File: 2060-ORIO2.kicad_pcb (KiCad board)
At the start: 4 copper layers, 100 x 100 mm, 198 parts, among them J11 RaspberryPI-B+header, J12 Conn_01x04, J13 Conn_01x08, J14 Conn_01x02, J15 Conn_01x08, J16 Conn_01x10, J17 Conn_01x10, J18 Conn_01x10, J19 Conn_01x10, J20 Conn_01x09, J21 Conn_01x08, J22 Conn_01x08, J23 Conn_01x08, J24 Conn_01x08, J25 Conn_01x08, J26 Conn_01x08, J28 Conn_01x16, J29 Conn_01x16, J30 Conn_01x16, J31 Conn_01x08, J32 Conn_01x08, J33 Conn_01x08, J34 Conn_01x08, J35 TBL001-500-02GY-2GY, Q11 ULN2803ADWR, Q12 BCV27, Q91 BCV27, Q92 BCV27, Q93 BCV27, Q94 BCV27, SW1 SW_DIP_x01, SW11 SW_DIP_x08, U1 AOZ2151TQI-19, U11 ICE40HX4K-TQ144, U12 ‎74LVT245B, U13 ‎74LVT245B, U14 ‎74LVT245B, U15 AOZ2151TQI-19, U16 MCP3008, U17 AZ1117CH-3.3TRG1, U18 AZ1117CH-3.3TRG1, U19 AZ1117CH-1.2, U20 AOZ2151TQI-19, U21 ‎74LVT245B, U22 ‎74LVT245B, U23 ‎74LVT245B, U24 ‎74LVT245B, U26 AP3012, Y11 XLH536025_000000I

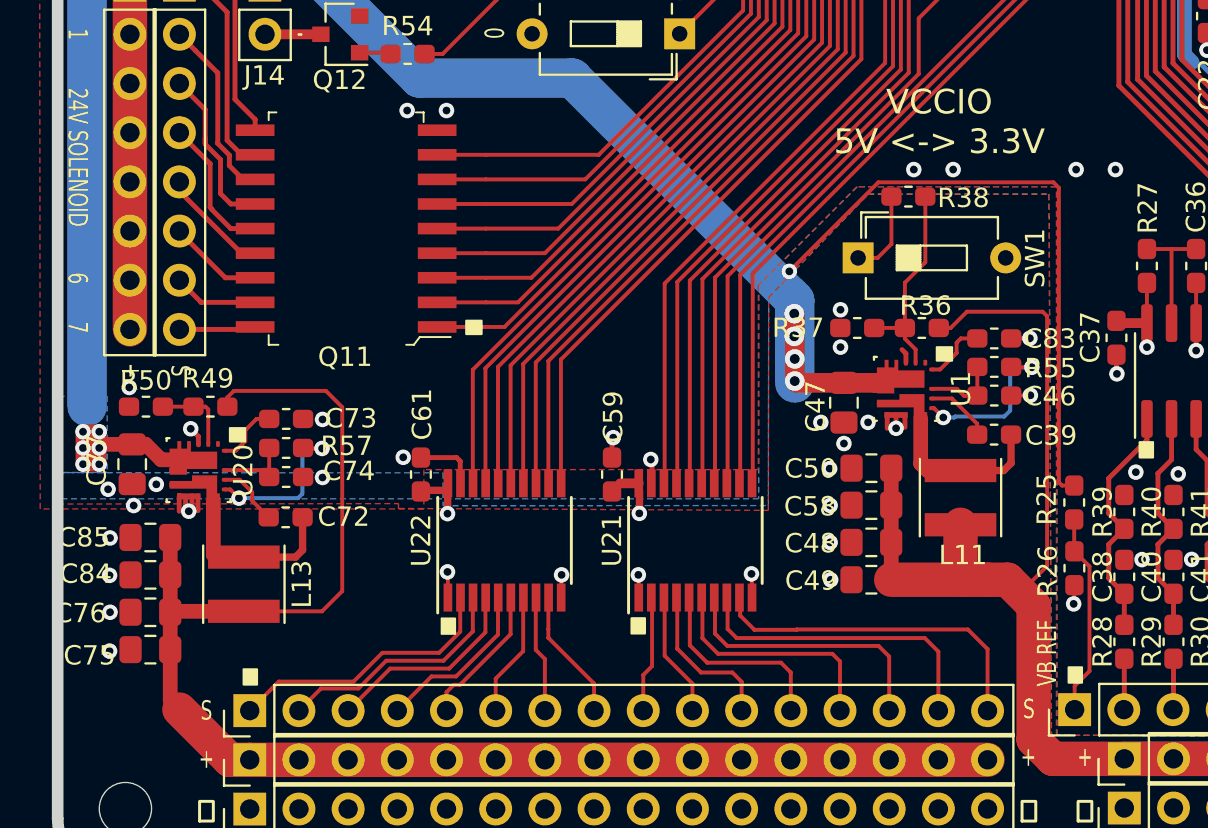
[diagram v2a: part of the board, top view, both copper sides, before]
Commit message: Change +BATT voltage divider to /6.
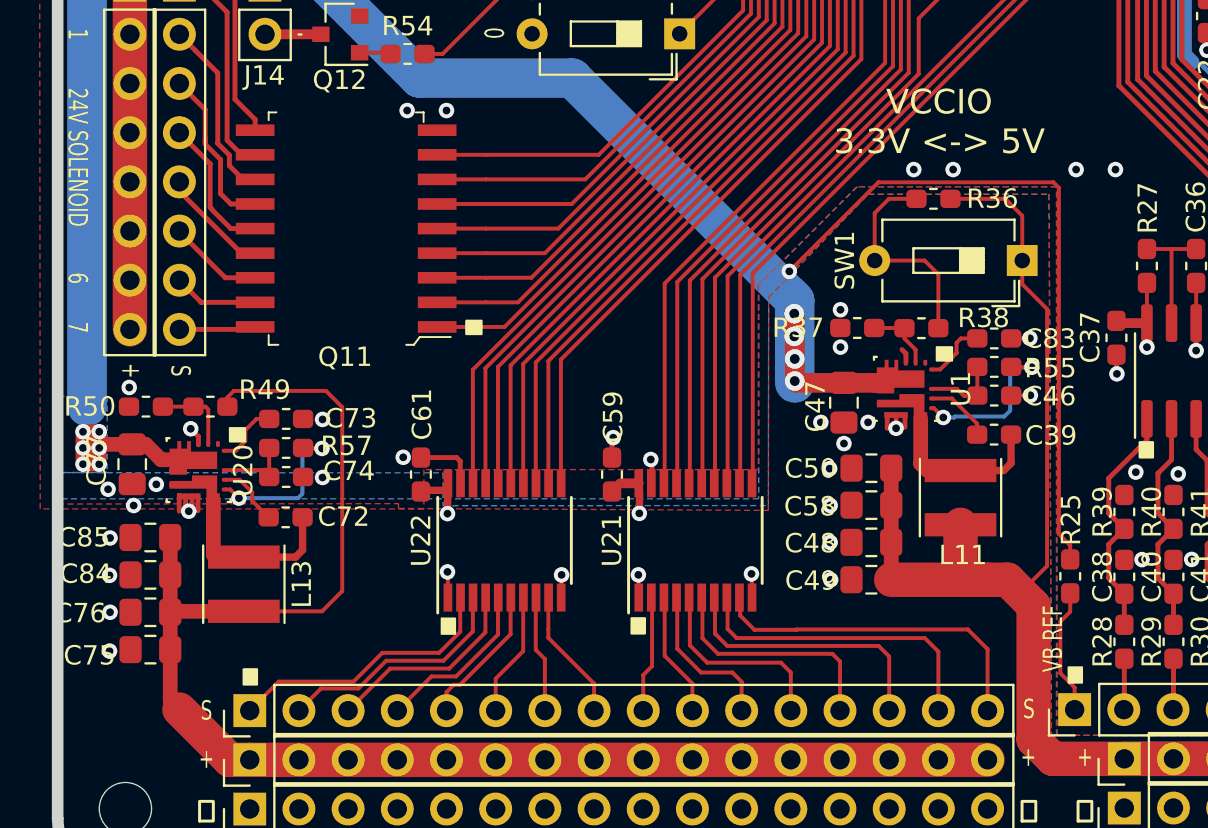
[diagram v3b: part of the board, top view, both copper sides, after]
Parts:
- removed R26: 3K3, Resistor_SMD:R_0603_1608Metric_Pad1.05x0.95mm_HandSolder
- R25: value 33K -> 18K8
- R36: value x -> 3K4
- R37, R48, R50: value x -> 1K6
- R38: value x -> 5K
- R47: value x -> 8K4
- R49: value x -> 10K4
- moved SW1 8.48 mm to (121.8, 110.2), turned to 180 degrees
- moved R38 6.83 mm to (116.6, 113.7)
- moved R36 6.69 mm to (117.2, 107.0), turned to 0 degrees
- moved R25 3.82 mm to (124.3, 126.5)
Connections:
- R36 pad 1: VCC_IO -> Net-(R36-Pad1)
- R36 pad 2: Net-(R36-Pad2) -> VCC_IO
- R37 pad 1: Net-(R36-Pad2) -> Net-(R37-Pad1)
- R38 pad 1: Net-(R38-Pad1) -> Net-(R37-Pad1)
- R38 pad 2: Net-(R36-Pad2) -> Net-(R36-Pad1)
- SW1 pad 1: Net-(R38-Pad1) -> VCC_IO
- SW1 pad 2: GND -> Net-(R36-Pad1)
- U1 pad 2: Net-(R36-Pad2) -> Net-(R37-Pad1)
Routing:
- net Net-(R36-Pad1): track 0.00 -> 11.3 mm
- net Net-(R36-Pad2): track 10.8 -> 0.00 mm
- net Net-(R38-Pad1): track 4.47 -> 0.00 mm
- net /VBATT_DIV: track 10.5 -> 6.52 mm
- net VCC_IO: track 314.0 -> 317.7 mm
- net Net-(R37-Pad1): track 0.00 -> 3.59 mm
- net +BATT: track 204.5 -> 207.9 mm
- net GND: track 112.0 -> 111.1 mm, vias 155 -> 154
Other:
- board text added: "VCCIO 3.3V <-> 5V"
- board text removed: "VCCIO 5V <-> 3.3V"

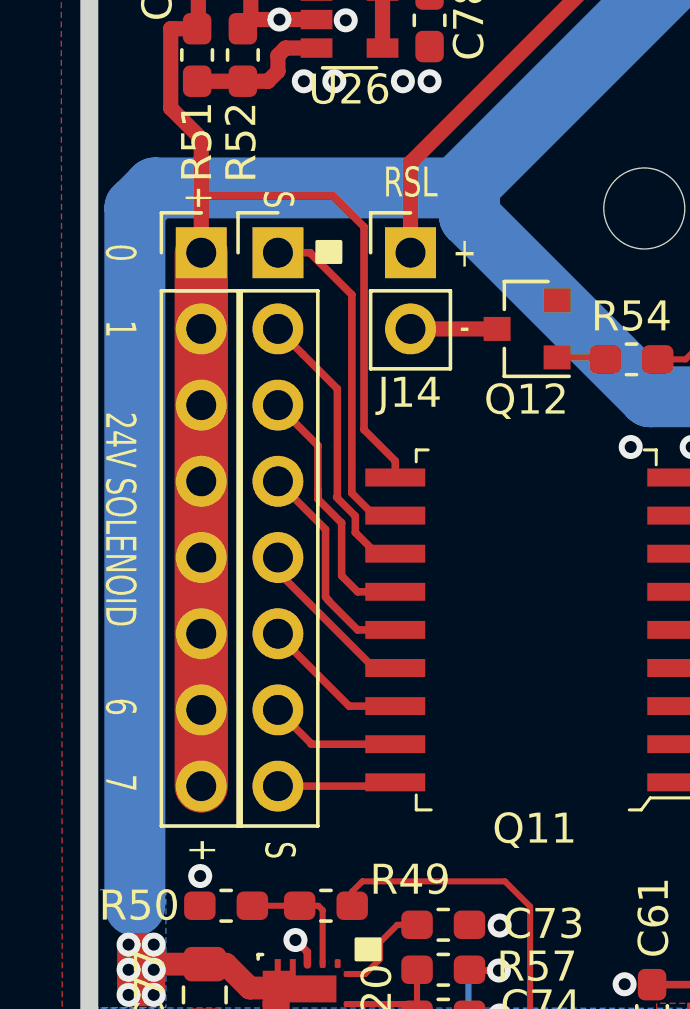
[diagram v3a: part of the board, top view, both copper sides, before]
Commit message: Adjust solenoid connector position.
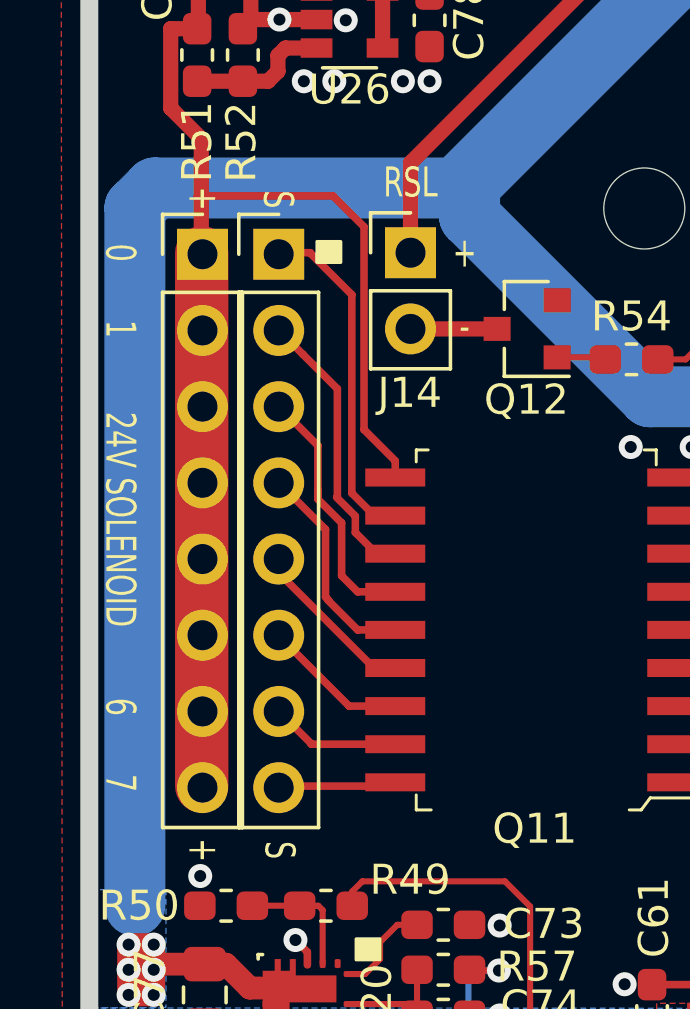
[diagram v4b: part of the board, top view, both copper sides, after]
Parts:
- R55, R56, R57: value x -> 0
- moved J13 0.07 mm to (75.8, 96.0)
- moved J15 0.06 mm to (78.3, 96.0)
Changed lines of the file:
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@@
-(kicad_pcb (version 20171130) (host pcbnew 5.1.6-c6e7f7d~87~ubuntu18.04.1)
+(kicad_pcb (version 20171130) (host pcbnew 5.1.5+dfsg1-2build2)
   (general
     (thickness 1.6)
     (drawings 165)
-    (tracks 2351)
+    (tracks 2352)
     (zones 0)
     (modules 197)
@@
       (effects (font (size 1 1) (thickness 0.15)))
     )
-    (fp_text value x (at 0 1.43) (layer F.Fab)
+    (fp_text value 0 (at 0 1.43) (layer F.Fab)
       (effects (font (size 1 1) (thickness 0.15)))
     )
@@
       (effects (font (size 1 1) (thickness 0.15)))
     )
-    (fp_text value x (at 0 1.43 90) (layer F.Fab)
+    (fp_text value 0 (at 0 1.43 90) (layer F.Fab)
       (effects (font (size 1 1) (thickness 0.15)))
     )
@@
       (effects (font (size 1 1) (thickness 0.15)))
     )
-    (fp_text value x (at 0 1.43) (layer F.Fab)
+    (fp_text value 0 (at 0 1.43) (layer F.Fab)
       (effects (font (size 1 1) (thickness 0.15)))
     )
@@
     )
   )
-  (module Connector_PinHeader_2.54mm:PinHeader_1x08_P2.54mm_Vertical (layer F.Cu)
-    (at 78.2878 95.975)
+  (module Connector_PinHeader_2.54mm:PinHeader_1x08_P2.54mm_Vertical locked (layer F.Cu)
+    (at 78.3132 96.0258)
     (descr "Through hole straight pin header, 1x08, 2.54mm pitch, single row")
     (tags "Through hole pin header THT 1x08 2.54mm single row")
@@
     )
   )
-  (module Connector_PinHeader_2.54mm:PinHeader_1x08_P2.54mm_Vertical (layer F.Cu)
-    (at 75.7326 95.975)
+  (module Connector_PinHeader_2.54mm:PinHeader_1x08_P2.54mm_Vertical locked (layer F.Cu)
+    (at 75.7732 96.0258)
     (descr "Through hole straight pin header, 1x08, 2.54mm pitch, single row")
     (tags "Through hole pin header THT 1x08 2.54mm single row")
@@
     (effects (font (size 1 0.7) (thickness 0.15)))
   )
-  (gr_text + (at 75.6716 94.1462 270) (layer F.SilkS)
+  (gr_text + (at 75.7986 94.1716 270) (layer F.SilkS)
     (effects (font (size 1 0.7) (thickness 0.15)))
   )
@@
   (segment (start 82.9323 44.8067) (end 84.5883 44.8067) (width 0.2032) (layer F.Cu) (net 278))
   (segment (start 83.6182 65.749) (end 86.238 65.749) (width 2.54) (layer F.Cu) (net 279))
-  (segment (start 75.7326 113.755) (end 75.7326 95.975) (width 1.778) (layer F.Cu) (net 280))
+  (segment (start 75.7478 113.755) (end 75.7478 95.975) (width 1.778) (layer F.Cu) (net 280))
   (segment (start 76.3574 85.221) (end 76.0878 85.221) (width 0.508) (layer F.Cu) (net 280))
   (segment (start 75.6348 85.674) (end 75.6348 86.958) (width 0.508) (layer F.Cu) (net 280))
@@
   (segment (start 75.5954 88.5087) (end 74.71399 88.5087) (width 0.508) (layer F.Cu) (net 280))
   (segment (start 75.7326 92.1752) (end 75.7326 94.0802) (width 0.508) (layer F.Cu) (net 280))
-  (segment (start 75.7326 94.0802) (end 75.7326 95.975) (width 0.508) (layer F.Cu) (net 280))
   (segment (start 82.1984 102.914) (end 82.1984 103.468) (width 0.254) (layer F.Cu) (net 280))
   (segment (start 81.158 101.8736) (end 82.1984 102.914) (width 0.254) (layer F.Cu) (net 280))
@@
   (segment (start 80.1268 94.0802) (end 81.158 95.1114) (width 0.254) (layer F.Cu) (net 280))
   (segment (start 75.7326 94.0802) (end 80.1268 94.0802) (width 0.254) (layer F.Cu) (net 280))
+  (segment (start 75.7326 95.4568) (end 75.2398 95.9496) (width 0.508) (layer F.Cu) (net 280))
+  (segment (start 75.7326 94.0802) (end 75.7326 95.4568) (width 0.508) (layer F.Cu) (net 280))
   (segment (start 82.7074 98.515) (end 85.5936 98.515) (width 0.508) (layer F.Cu) (net 281))
   (segment (start 89.1324 99.465) (end 89.1984 99.531) (width 0.2032) (layer F.Cu) (net 282))

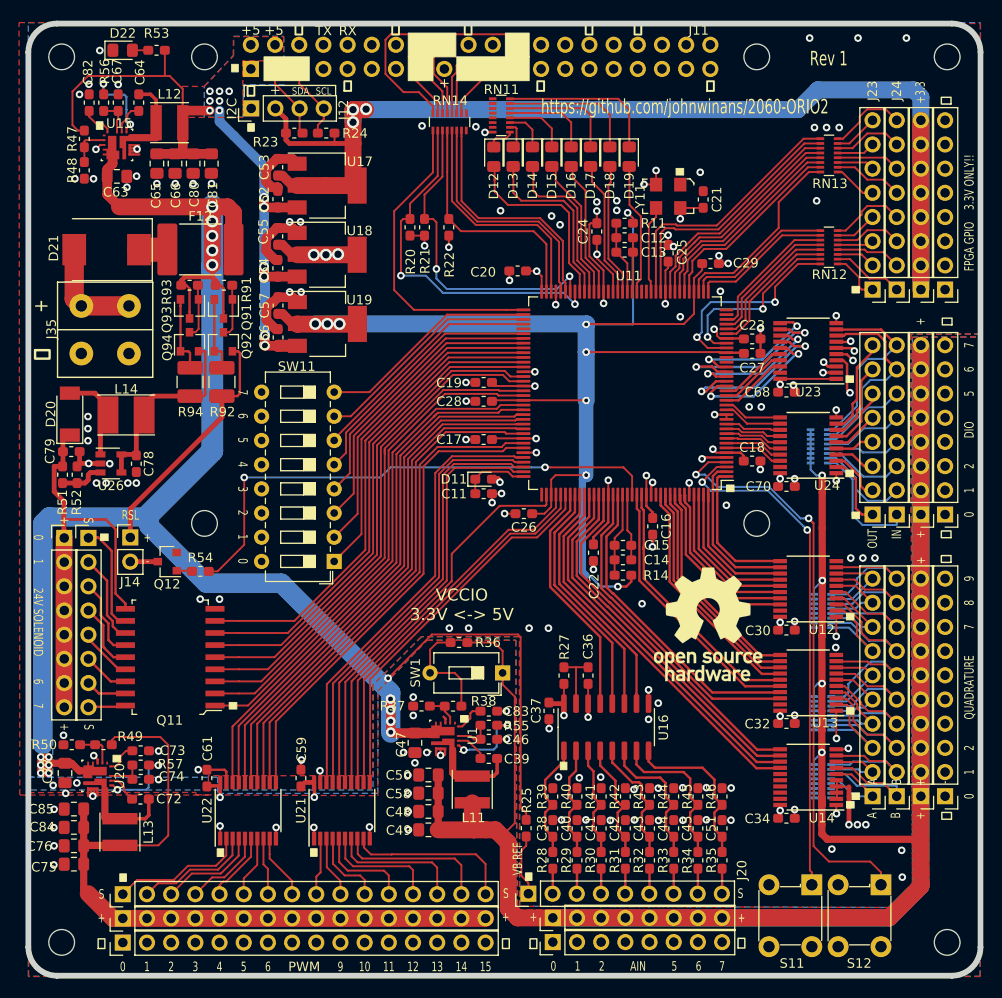
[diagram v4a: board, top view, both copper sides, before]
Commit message: Replace AOZ2151TQI-19 regulators with AP63300WU-7
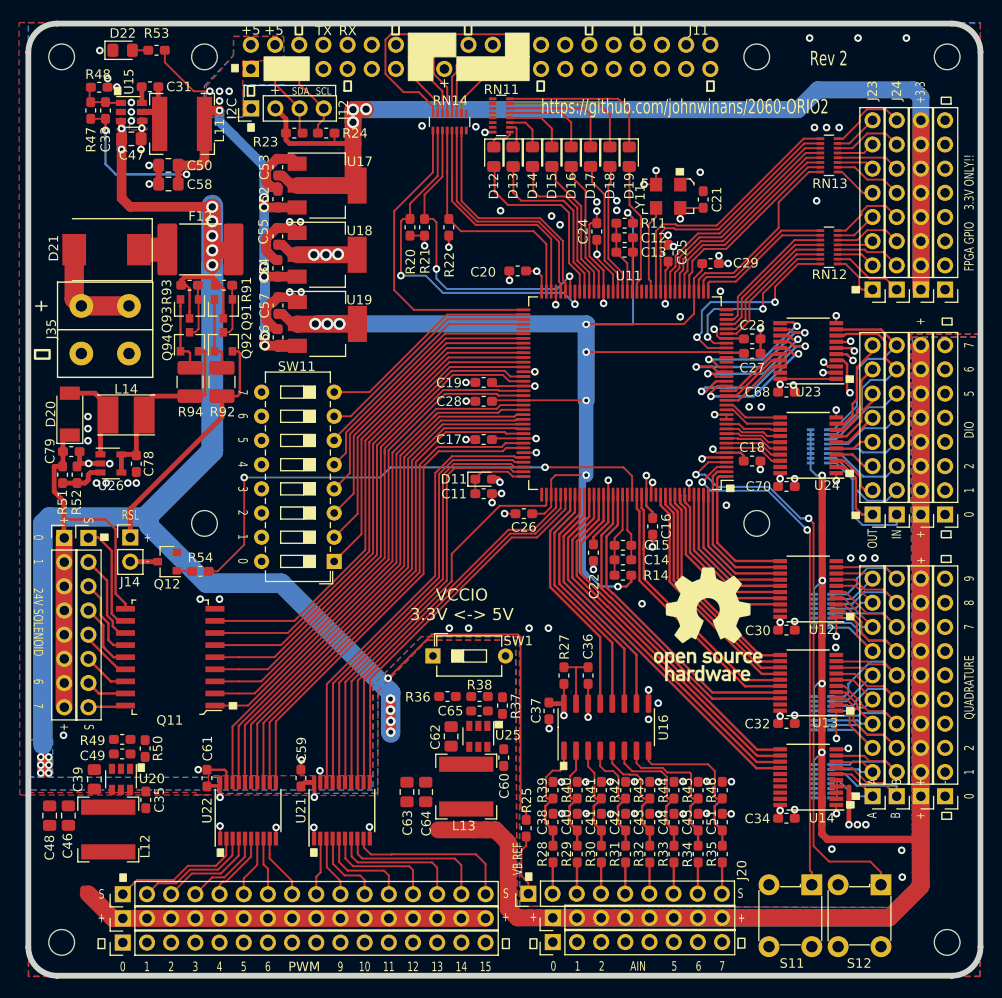
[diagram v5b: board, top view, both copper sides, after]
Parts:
- removed C66, C75, C76, C77, C80, C81, C84, C85: 22uF, Capacitor_SMD:C_0805_2012Metric_Pad1.15x1.40mm_HandSolder
- removed C67, C74: 4.7uF, Capacitor_SMD:C_0603_1608Metric_Pad1.05x0.95mm_HandSolder
- removed C72: .1uF, Capacitor_SMD:C_0603_1608Metric_Pad1.05x0.95mm_HandSolder
- removed C73, C82, C83: .001uF, Capacitor_SMD:C_0603_1608Metric_Pad1.05x0.95mm_HandSolder
- removed R55, R56, R57: 0, Resistor_SMD:R_0603_1608Metric_Pad1.05x0.95mm_HandSolder
- removed U1: AOZ2151TQI-19, jb-footprint:AOZ2151TQI-19
- added C31: .1uF, Capacitor_SMD:C_0603_1608Metric_Pad1.05x0.95mm_HandSolder, F.Cu at (84.8, 48.6)
- added C33: 47pF, Capacitor_SMD:C_0603_1608Metric_Pad1.05x0.95mm_HandSolder, F.Cu at (80.1, 51.1)
- added C35: .1uF, Capacitor_SMD:C_0603_1608Metric_Pad1.05x0.95mm_HandSolder, F.Cu at (84.3, 123.5)
- added C60: .1uF, Capacitor_SMD:C_0603_1608Metric_Pad1.05x0.95mm_HandSolder, F.Cu at (121.9, 119.1)
- added C62: 10uF, Capacitor_SMD:C_0805_2012Metric_Pad1.15x1.40mm_HandSolder, F.Cu at (116.4, 116.9)
- added U25: AP63300, Package_TO_SOT_SMD:SOT-23-6, F.Cu at (119.3, 116.9)
- C39: value .1uF -> 10uF; footprint Capacitor_SMD:C_0603_1608Metric_Pad1.05x0.95mm_HandSolder -> Capacitor_SMD:C_0805_2012Metric_Pad1.15x1.40mm_HandSolder
- C46: value 4.7uF -> 22uF; footprint Capacitor_SMD:C_0603_1608Metric_Pad1.05x0.95mm_HandSolder -> Capacitor_SMD:C_0805_2012Metric_Pad1.15x1.40mm_HandSolder
- C47: value 22uF -> 10uF
- C49, C65: value 22uF -> 47pF; footprint Capacitor_SMD:C_0805_2012Metric_Pad1.15x1.40mm_HandSolder -> Capacitor_SMD:C_0603_1608Metric_Pad1.05x0.95mm_HandSolder
- C64: value .1uF -> 22uF; footprint Capacitor_SMD:C_0603_1608Metric_Pad1.05x0.95mm_HandSolder -> Capacitor_SMD:C_0805_2012Metric_Pad1.15x1.40mm_HandSolder
- L11, L12, L13: value 2.2uH -> 6.8uH; footprint Inductor_SMD:L_Taiyo-Yuden_MD-4040 -> Inductor_SMD:L_Bourns-SRN6028
- U15, U20: value AOZ2151TQI-19 -> AP63300; footprint jb-footprint:AOZ2151TQI-19 -> Package_TO_SOT_SMD:SOT-23-6
- moved C64 78.4 mm to (113.7, 122.7)
- moved L11 76.3 mm to (88.1, 52.5), turned to 0 degrees
- moved L12 74.5 mm to (80.4, 126.6), turned to 270 degrees
- moved C63 71.5 mm to (111.8, 122.7), turned to 90 degrees
- moved C47 70.1 mm to (82.8, 54.1), turned to 0 degrees
- moved C50 69.6 mm to (86.7, 56.9)
- moved C58 69.6 mm to (86.7, 58.9)
- moved C65 66.7 mm to (119.4, 114.2), turned to 0 degrees
- moved C46 44.9 mm to (76.2, 125.2), turned to 90 degrees
- moved C39 41.5 mm to (78.9, 121.4), turned to 270 degrees
- moved C48 39.8 mm to (74.2, 125.2), turned to 90 degrees
- moved L13 36.7 mm to (118.0, 122.1)
- moved C49 33.1 mm to (81.9, 118.7), turned to 0 degrees
- moved R48 8.86 mm to (79.4, 48.7), turned to 0 degrees
- moved R37 8.51 mm to (121.8, 113.6), turned to 270 degrees
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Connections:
- C39 pad 1: Net-(C39-Pad1) -> +BATT
- C39 pad 2: Net-(C39-Pad2) -> GND
- C46 pad 1: Net-(C46-Pad1) -> VCC_PWM
- C48 pad 1: VCC_IO -> VCC_PWM
- C49 pad 1: VCC_IO -> VCC_PWM
- C49 pad 2: GND -> Net-(C49-Pad2)
- C50 pad 1: VCC_IO -> 5V_PI
- C58 pad 1: VCC_IO -> 5V_PI
- C63 pad 1: +BATT -> VCC_IO
- C64 pad 1: Net-(C64-Pad1) -> VCC_IO
- C64 pad 2: Net-(C64-Pad2) -> GND
- C65 pad 1: 5V_PI -> VCC_IO
- C65 pad 2: GND -> Net-(C65-Pad2)
- L11 pad 1: Net-(C39-Pad2) -> Net-(C31-Pad2)
- L11 pad 2: VCC_IO -> 5V_PI
- L12 pad 1: Net-(C64-Pad2) -> Net-(C35-Pad2)
- L12 pad 2: 5V_PI -> VCC_PWM
- L13 pad 1: Net-(C72-Pad2) -> Net-(C60-Pad2)
- L13 pad 2: VCC_PWM -> VCC_IO
- R37 pad 1: Net-(R37-Pad1) -> Net-(C65-Pad2)
- R38 pad 1: Net-(R37-Pad1) -> Net-(C65-Pad2)
- R47 pad 2: Net-(R47-Pad2) -> Net-(C33-Pad2)
- R48 pad 1: Net-(R47-Pad2) -> Net-(C33-Pad2)
- R49 pad 2: Net-(R49-Pad2) -> Net-(C49-Pad2)
- R50 pad 1: Net-(R49-Pad2) -> Net-(C49-Pad2)
- U15 pad 1: Net-(U15-Pad1) -> Net-(C33-Pad2)
- U15 pad 2: Net-(R47-Pad2) -> Net-(U15-Pad2)
- U15 pad 3: GND -> +BATT
- U15 pad 4: +BATT -> GND
- U20 pad 1: Net-(U20-Pad1) -> Net-(C49-Pad2)
- U20 pad 2: Net-(R49-Pad2) -> Net-(U20-Pad2)
- U20 pad 3: GND -> +BATT
- U20 pad 4: +BATT -> GND
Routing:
- net VCC_PWM: track 77.6 -> 43.5 mm
- net VCC_IO: track 317.7 -> 284.4 mm
- net Net-(C72-Pad2): track 12.0 -> 0.00 mm
- net +BATT: track 207.9 -> 196.5 mm, vias 16 -> 18
- net Net-(C64-Pad2): track 11.4 -> 0.00 mm
- net Net-(R36-Pad1): track 11.3 -> 0.00 mm
- net Net-(C39-Pad2): track 9.33 -> 0.00 mm
- net Net-(R55-Pad2): track 8.63 -> 0.00 mm, vias 2 -> 0
- net Net-(R56-Pad2): track 8.63 -> 0.00 mm, vias 2 -> 0
- net Net-(R57-Pad2): track 8.42 -> 0.00 mm, vias 2 -> 0
- net Net-(C31-Pad2): track 0.00 -> 5.00 mm
- net Net-(C33-Pad2): track 0.00 -> 4.81 mm
- net Net-(R47-Pad2): track 4.31 -> 0.00 mm
- net Net-(R49-Pad2): track 4.18 -> 0.00 mm
- net GND: track 111.1 -> 107.0 mm, vias 154 -> 127
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- added copper zone on In1.Cu, net +BATT
- added copper zone on In2.Cu, net +BATT
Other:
- board text added: "Rev 2"
- board text removed: "Rev 1"
